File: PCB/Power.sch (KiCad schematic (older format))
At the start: 19 parts, among them J1 B2B-PH-K-S(LF)(SN), J2 B3B-PH-K-S(LF)(SN), Q1 DMG2307L-7, Q2 DMG2307L-7, SW3 CUS-12TB, U1 BQ24210DQCT, U2 AZ1117CR-3.3TRG1_1

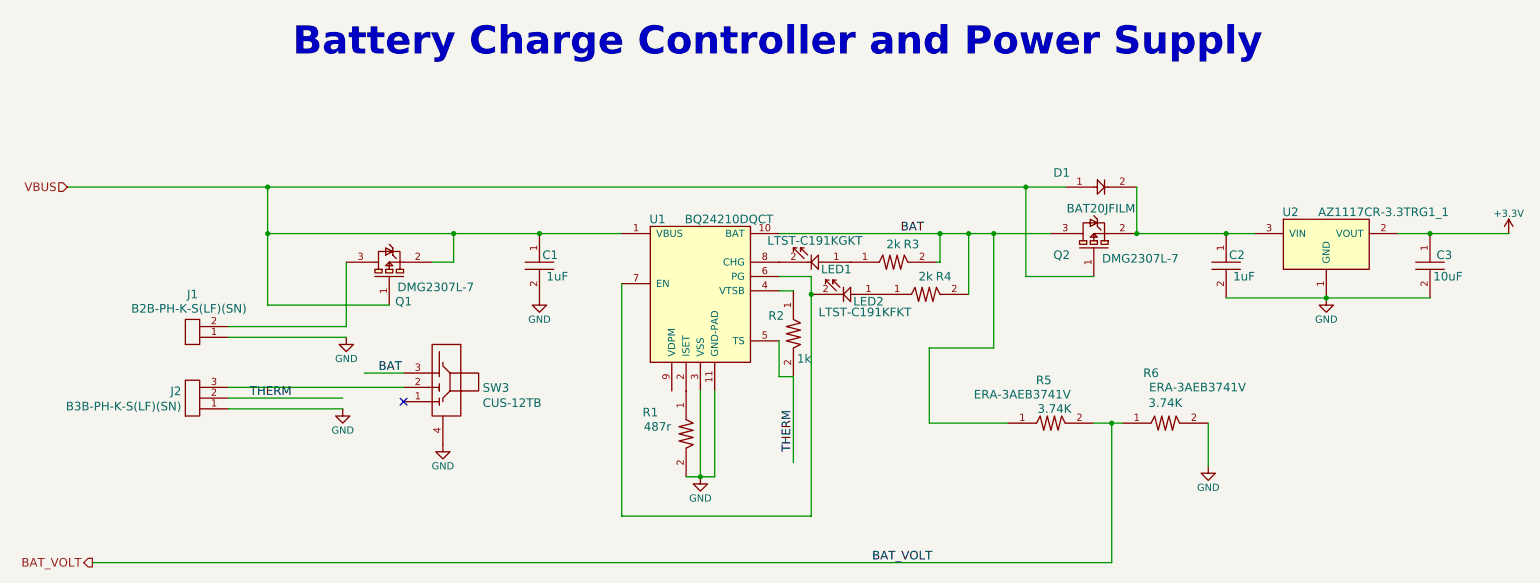
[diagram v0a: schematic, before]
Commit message: Initial commit
Project created in KicAD< scheamtic near complete, components for sub
1GHZ RF system added to related libaries. Datasheets for components
added.
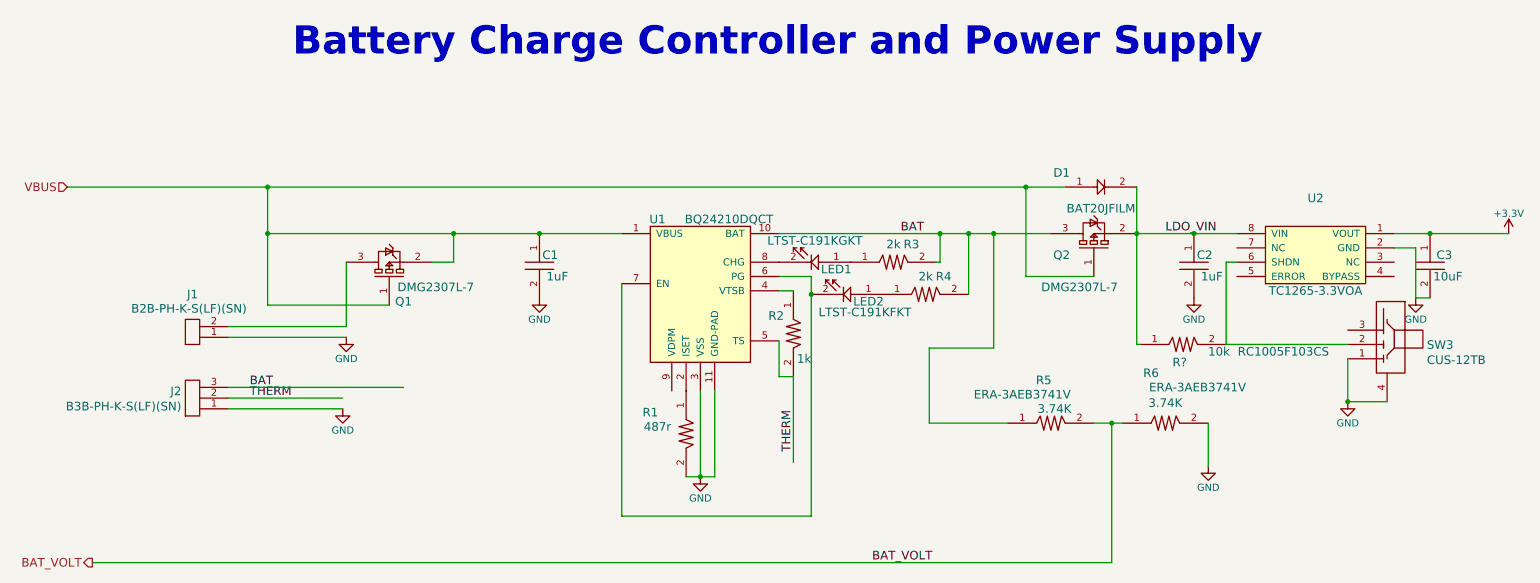
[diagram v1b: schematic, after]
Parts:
- removed U2: AZ1117CR-3.3TRG1_1, PCB_Footprints:AZ1117CR-3.3TRG1, symbol AZ1117CR-3.3TRG1_1
- added R?: RC1005F103CS, PCB_Footprints:R0402, symbol RC1005F103CS
- added U2: TC1265-3.3VOA, PCB_Footprints:TC1265-3.3VOA, symbol TC1265-3.3VOA
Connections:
- net labels added: LDO_VIN
- wire segments 42 -> 50
- no-connect marks 1 -> 0
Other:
- moved on the sheet: C2, SW3
